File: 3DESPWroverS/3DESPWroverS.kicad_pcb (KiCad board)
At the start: 2 copper layers, 40 x 40 mm, 9 parts, among them J1 Conn_02x03_Odd_Even, J2 Conn_01x01, J3 Conn_01x01, J4 Conn_01x01, J5 Conn_01x01, J6 Conn_01x01, J7 Conn_01x01, J8 Conn_01x01, J9 Conn_01x01

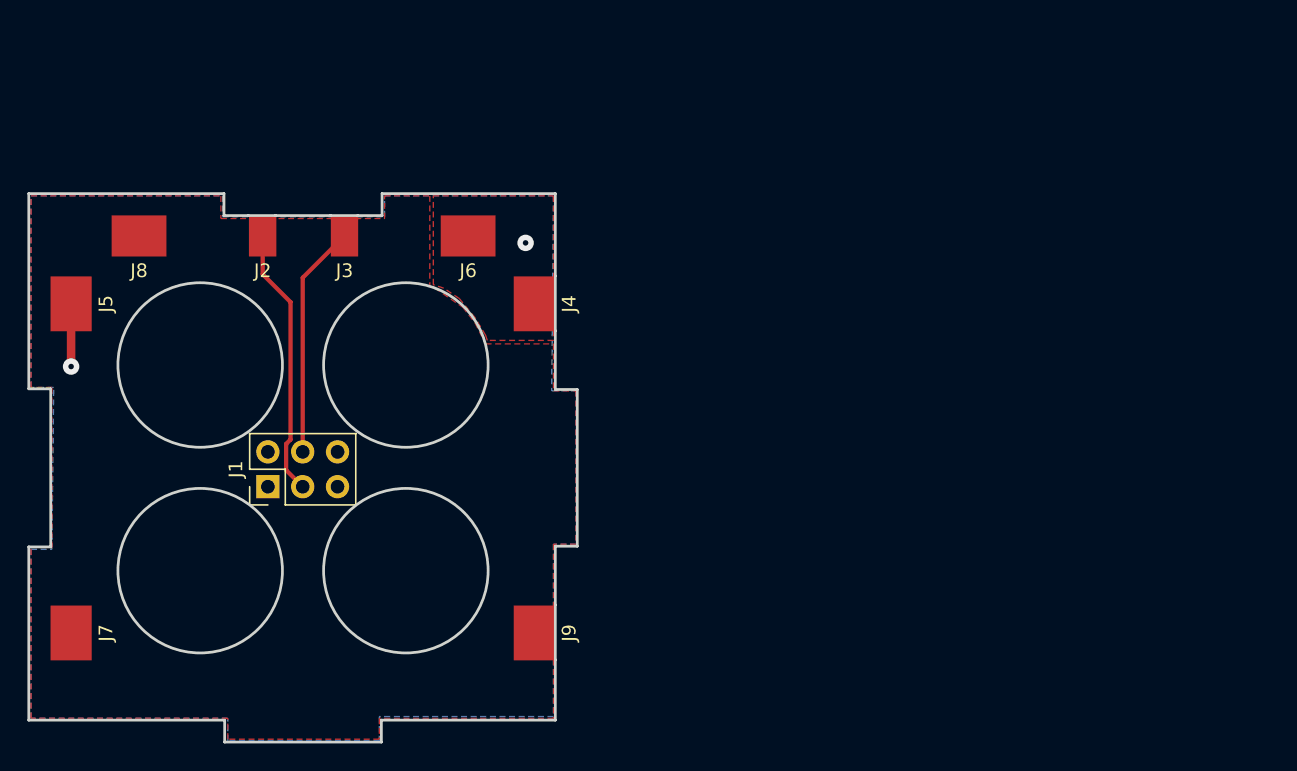
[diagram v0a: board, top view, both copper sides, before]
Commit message: Made corrections and added holes for zipties/nylon
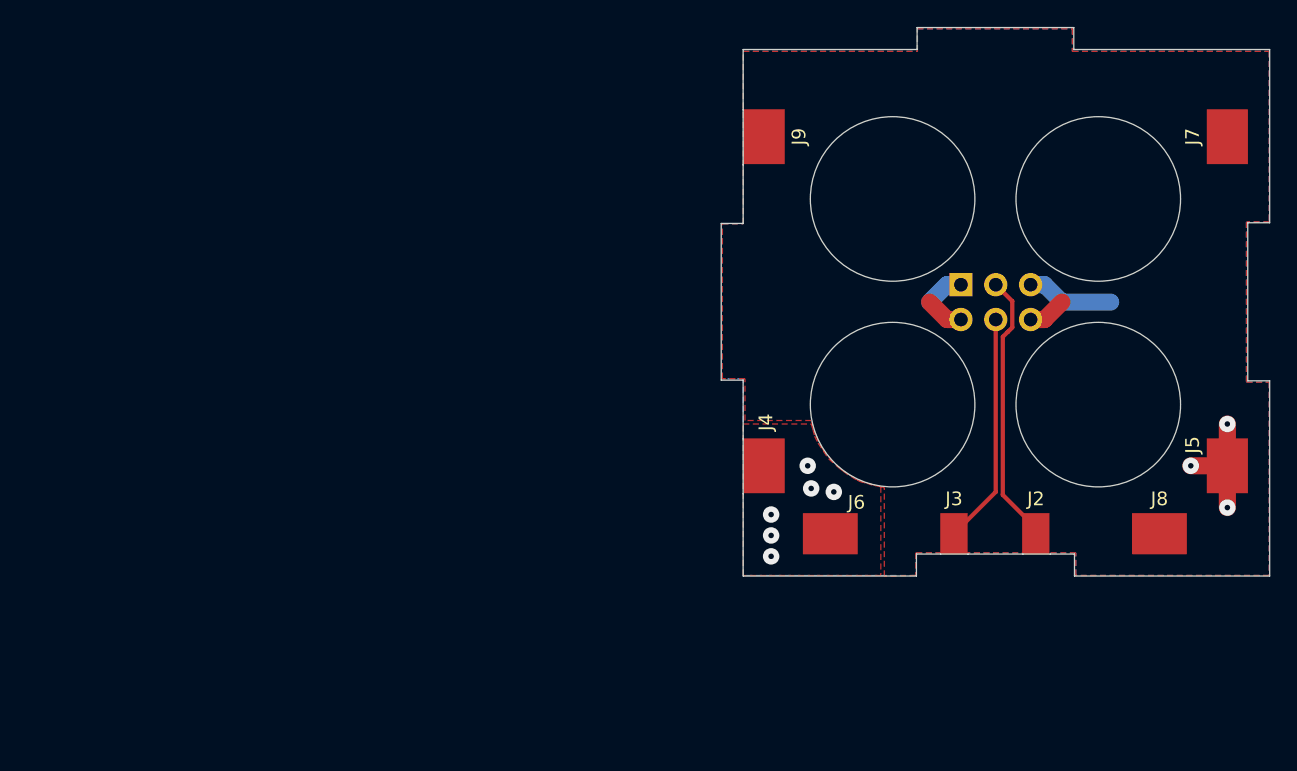
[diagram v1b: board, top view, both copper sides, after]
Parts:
- J1: moved to B.Cu
- moved J7 91.8 mm to (137.4, 45.8), turned to 270 degrees
- moved J5 85.2 mm to (137.4, 69.8), turned to 270 degrees
- moved J8 77.5 mm to (132.5, 74.8), turned to 180 degrees
- moved J2 60.4 mm to (123.4, 74.8), turned to 180 degrees
- moved J1 52.6 mm to (118.0, 56.6), turned to 270 degrees
- moved J3 49.5 mm to (117.5, 74.8), turned to 180 degrees
- moved J9 39.9 mm to (103.6, 45.8), turned to 270 degrees
- moved J6 34.2 mm to (108.5, 74.8), turned to 180 degrees
- moved J4 20.5 mm to (103.6, 69.8), turned to 270 degrees
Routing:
- net VCC: track 4.57 -> 17.9 mm, vias 2 -> 9
- net GND: track 0.00 -> 5.62 mm
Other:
- outline, holes or cut-outs redrawn
- net class Power: trace_width 0.625 -> 1.25
- board text added: "Project Cube, v1.1 REAL, ITU rodr"
